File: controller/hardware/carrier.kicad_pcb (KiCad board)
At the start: 2 copper layers, 160 x 60 mm, 52 parts, among them J1 6P6C, J10 WIZ850io J1 (SPI), J11 WIZ850io J2 (power, reset), J2 6P6C, J3 6P6C, J4 6P6C, J5 8P8C, J6 Panel DC in, 2.1 mm, U1 THVD1410, U2 THVD1410, U3 THVD1410, U4 THVD1410, U5 THVD1410

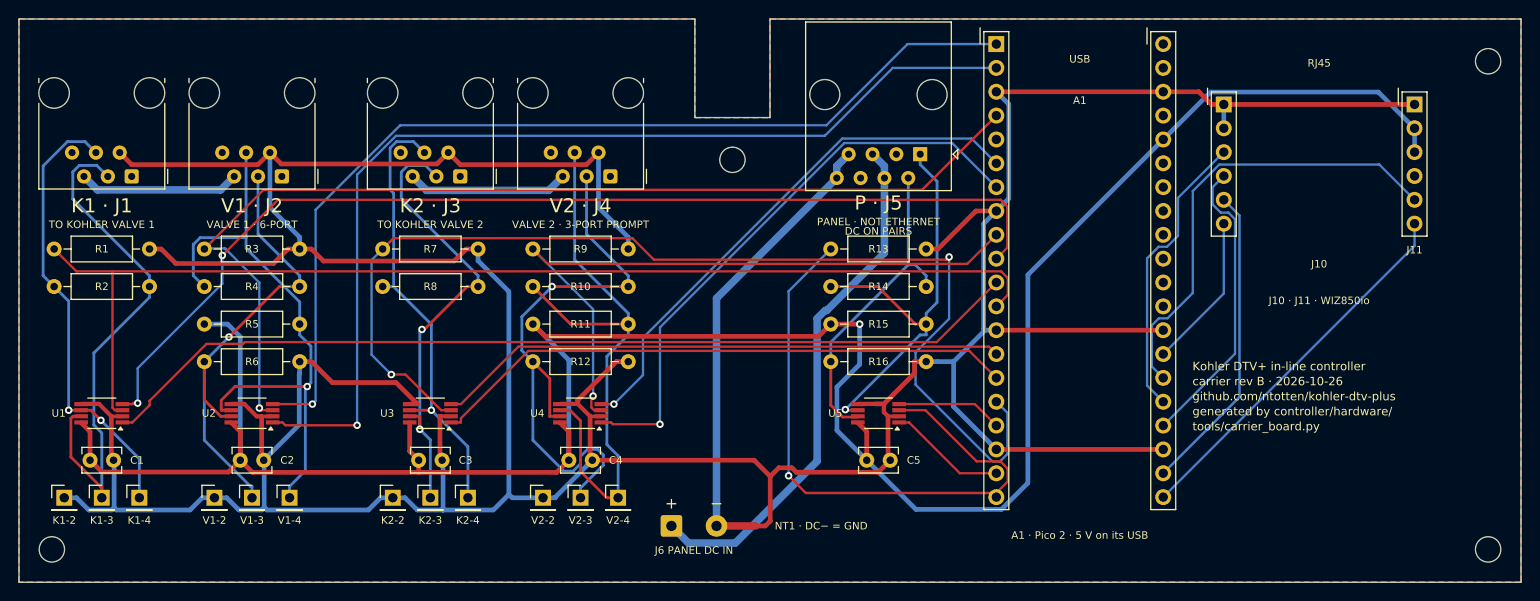
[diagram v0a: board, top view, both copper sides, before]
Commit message: Carrier PCB: valve jacks back to the Würth 615006138421
The board's four valve jacks were the Amphenol 54601-906LF, picked this
morning because KiCad has a footprint for it. Mouser lists it obsolete
(discontinuance notice 2024-01-15), so the board goes back to the Würth
615006138421 already in the order.

Its footprint is new, written by carrier_footprints.py from Würth's data
sheet, rev 001.001: six 0.9 mm holes at 1.02 mm pitch in two rows 2.54 mm
apart, two 2.36 mm unplated pegs 12 mm apart. The mouth is taken as the peg
side, 6 mm ahead of the pegs, read from the drawings rather than measured.
The jack rows move so each mouth stays on the board edge; the port columns
don't change. Rerouted: 0 DRC violations, 0 unconnected, and a second run
reproduces every file byte for byte.

The shopping list drops what the corrected cart dropped (the 2x6 socket,
the Adafruit adapters, the Perma-Proto), records that the order hasn't been
placed, notes the Mouser lifecycle check of every board part, and marks the
PCB ready to order.

Co-Authored-By: Claude Opus 5.5 (1M context) <noreply@anthropic.com>
Claude-Session: https://claude.ai/code/session_01PNaoTTizvWnVxnC9Mh2V5e
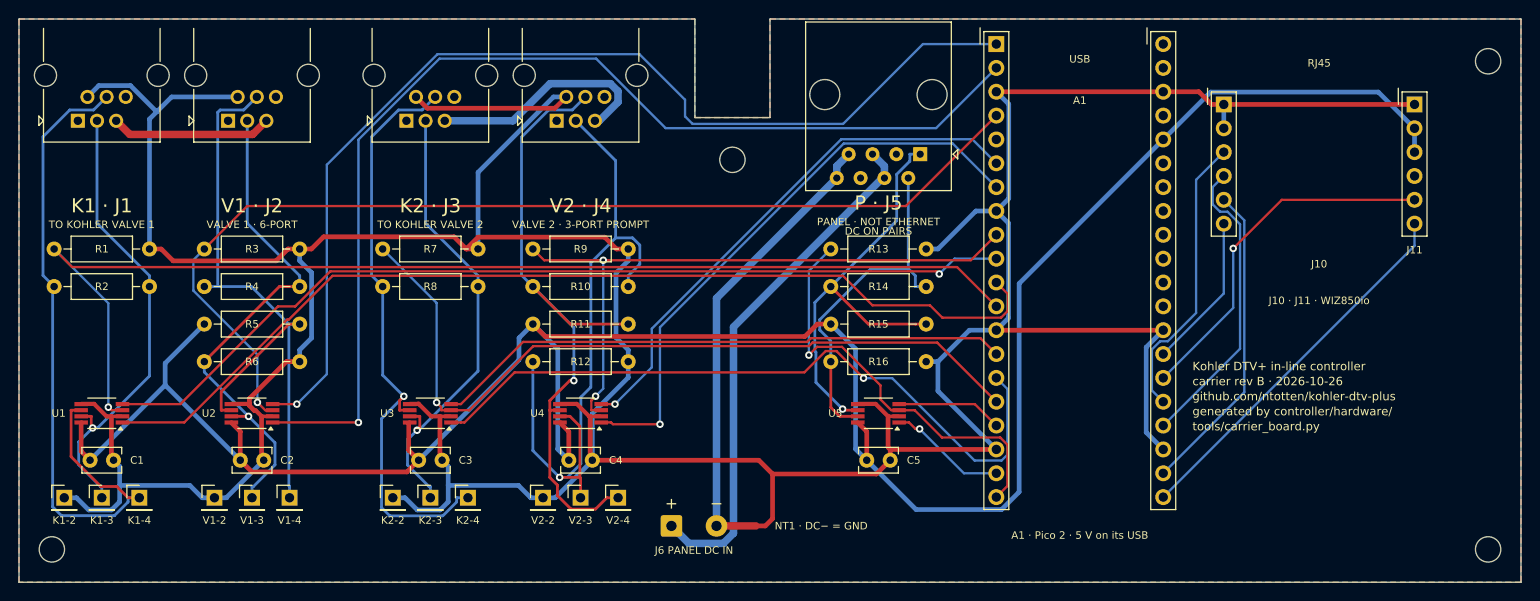
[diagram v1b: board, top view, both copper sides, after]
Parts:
- J1, J2, J3, J4: footprint Connector_RJ:RJ12_Amphenol_54601-x06_Horizontal -> carrier:RJ12_Wurth_615006138421_Horizontal
- moved J1 8.25 mm to (6.27, 10.8)
- moved J2 8.25 mm to (22.3, 10.8)
- moved J3 8.25 mm to (41.3, 10.8)
- moved J4 8.25 mm to (57.3, 10.8)
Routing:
- net /K2_DE: track 119.2 -> 84.5 mm, vias 2 -> 1
- net /K1_A: track 48.2 -> 74.3 mm, vias 2 -> 0
- net /P_DE: track 66.6 -> 45.0 mm
- net GND: track 485.4 -> 466.5 mm
- net /K2_A: track 48.6 -> 63.8 mm
- net /K1_TX: track 113.6 -> 99.7 mm, vias 2 -> 1
- net /K2_RX: track 62.7 -> 76.2 mm, vias 0 -> 1
- net /V2_B: track 63.7 -> 76.4 mm
- net /ETH_RST: track 49.1 -> 38.3 mm, vias 0 -> 1
- net /V1_TX: track 104.9 -> 113.2 mm
- net /V1_RX: track 108.6 -> 116.5 mm
- net /VALVE2_12V7: track 17.2 -> 24.9 mm
- net /K1_B: track 56.5 -> 49.4 mm, vias 0 -> 1
- net /K1_RX: track 99.5 -> 106.5 mm
- net /V2_A: track 65.6 -> 71.2 mm, vias 0 -> 1
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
